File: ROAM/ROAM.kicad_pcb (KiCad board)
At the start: 4 copper layers, 90 x 56.8 mm, 11 parts, among them J1 CommanderX16Expansion Alt, U1 SST39SF040 (ROM), U2 74HCT00, U3 74HCT138, U4 AS6C4008 (RAM)

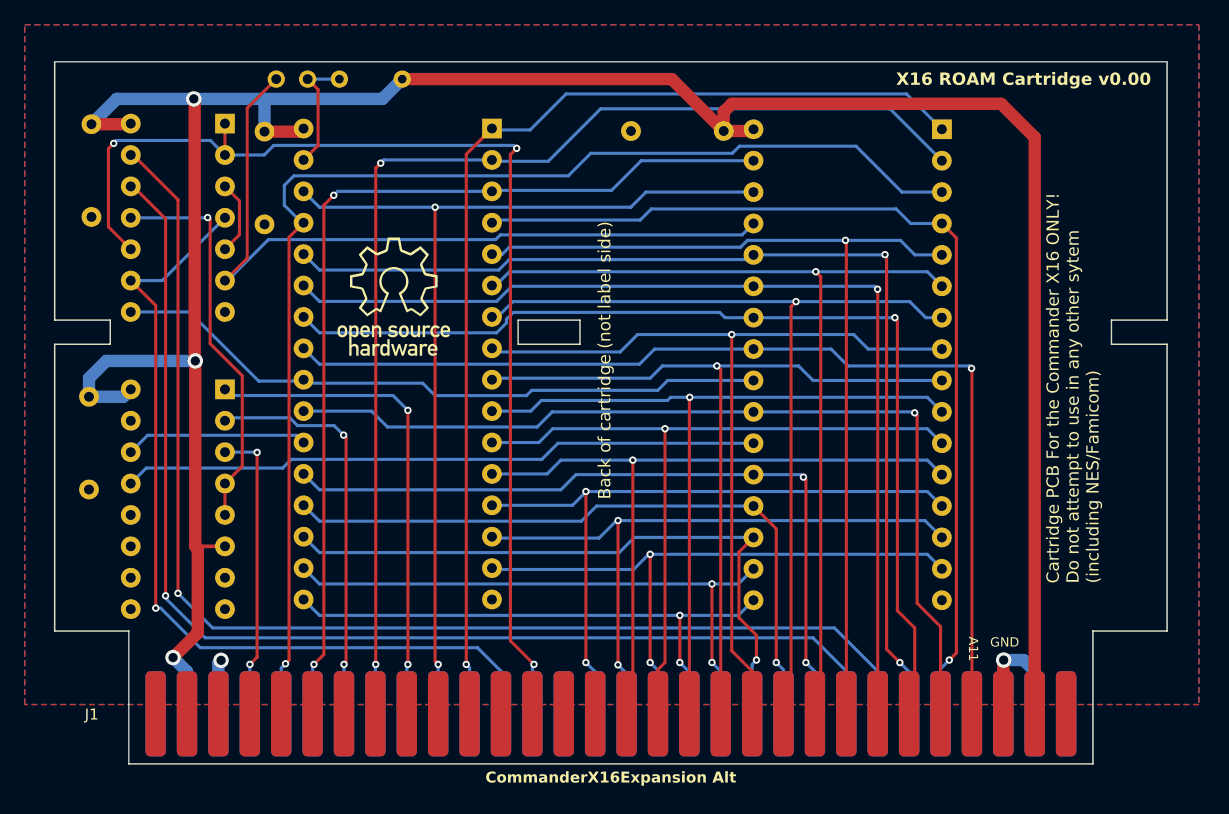
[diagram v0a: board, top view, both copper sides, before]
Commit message: Merged Wavicle's contributions to ROAM, added silk and some markup, updated readmed
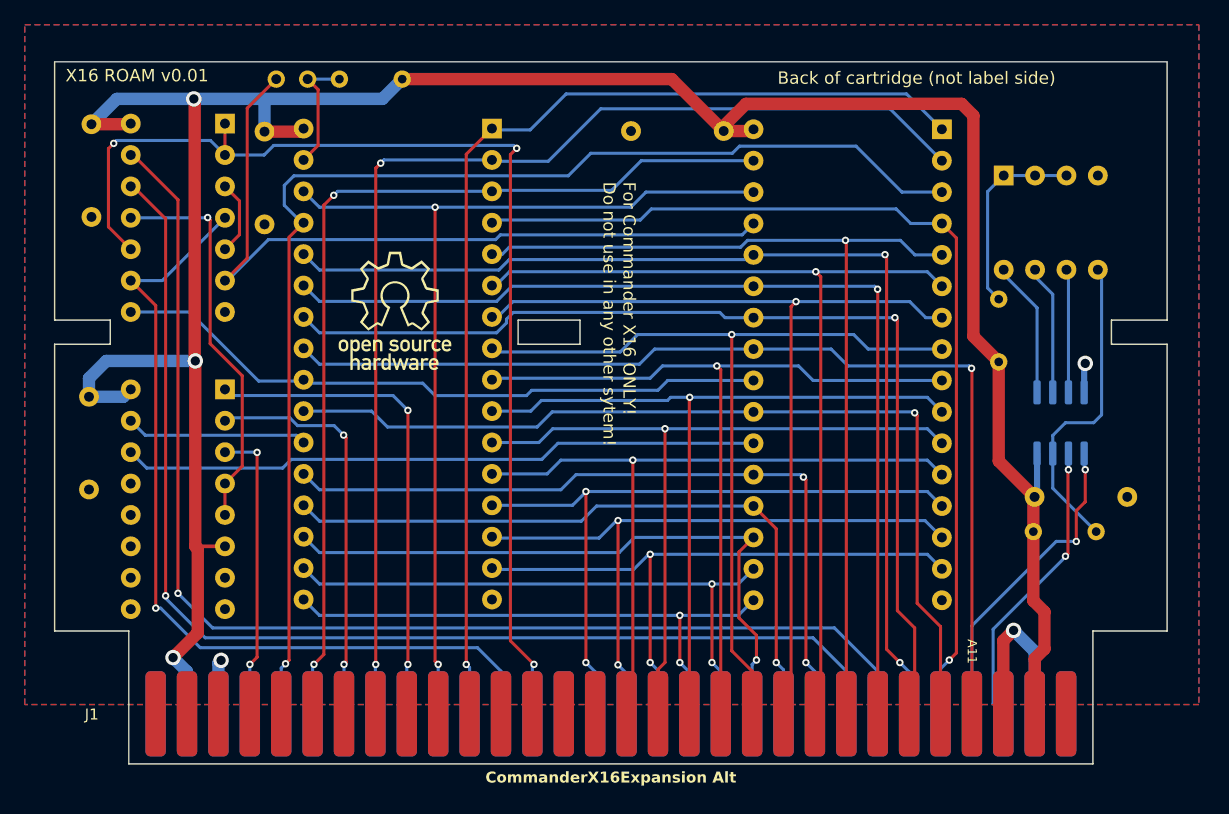
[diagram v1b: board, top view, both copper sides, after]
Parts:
- added C5: 100nF, Capacitor_THT:C_Axial_L3.8mm_D2.6mm_P7.50mm_Horizontal, B.Cu at (134.2, 113.2)
- added R2: 100K, Resistor_THT:R_Axial_DIN0204_L3.6mm_D1.6mm_P5.08mm_Horizontal, B.Cu at (131.7, 116.0)
- added R3: 100K, Resistor_THT:R_Axial_DIN0204_L3.6mm_D1.6mm_P5.08mm_Horizontal, B.Cu at (123.8, 102.3)
- added SW1: SW_DIP_x04, Button_Switch_THT:SW_DIP_SPSTx04_Slide_9.78x12.34mm_W7.62mm_P2.54mm, B.Cu at (124.2, 87.2)
- added U5: FM24C64B, Package_SO:SOIC-8_3.9x4.9mm_P1.27mm, B.Cu at (128.8, 107.2)
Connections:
- J1 pad 54: unconnected-(J1-SDA-Pad54) -> /SDA
- J1 pad 56: unconnected-(J1-SCL-Pad56) -> /SCL
- U3 pad 13: !RAMBEN -> unconnected-(U3-~{Y2}-Pad13)
- U3 pad 14: !ROMBEN -> !RAMBEN
- U3 pad 15: unconnected-(U3-~{Y0}-Pad15) -> !ROMBEN
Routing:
- net /SDA: track 0.00 -> 25.8 mm, vias 0 -> 2
- net /WP: track 0.00 -> 25.7 mm
- net /SCL: track 0.00 -> 23.6 mm, vias 0 -> 2
- net Net-(R3-Pad2): track 0.00 -> 16.0 mm
- net /FA0: track 0.00 -> 11.0 mm
- net /FA1: track 0.00 -> 10.5 mm
- net /FA2: track 0.00 -> 9.99 mm
- net GND: track 15.1 -> 21.3 mm, vias 2 -> 3
- net +5V: track 208.5 -> 210.3 mm
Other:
- board text added: "A0"
- board text added: "A1"
- board text added: "A2"
- board text added: "For Commander X16 ONLY! Do not use in any other sytem!"
- board text added: "NVRAM Addr"
- board text added: "NVRAM Wr. Prot."
- board text added: "X16 ROAM v0.01"
- board text removed: "Cartridge PCB For the Commander X16 ONLY! Do not attempt to use in any other sytem (including NES/Famicom)"
- board text removed: "GND"
- board text removed: "SCL"
- board text removed: "X16 ROAM Cartridge v0.00"

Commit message: Silk
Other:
- board text added: "5V"
- board text added: "A10"
- board text added: "A12"
- board text added: "A13"
- board text added: "A14"
- board text added: "A15"
- board text added: "A3"
- board text added: "A4"
- board text added: "A5"
- board text added: "A6"
- board text added: "A7"
- board text added: "A8"
- board text added: "A9"
- board text added: "D0"
- board text added: "D1"
- board text added: "D2"
- board text added: "D3"
- board text added: "D4"
- board text added: "D5"
- board text added: "D6"
- board text added: "D7"
- board text added: "Front of Cart Label side"
- board text added: "GND"
- board text added: "PHI2"
- board text added: "ROMB0"
- board text added: "ROMB1"
- board text added: "ROMB2"
- board text added: "ROMB3"
- board text added: "ROMB4"
- board text added: "ROMB5"
- board text added: "ROMB6"
- board text added: "ROMB7"
- board text added: "RWB"
- board text added: "SCL"
- board text added: "SDA"
- board text removed: "Front of cartridge, label side"

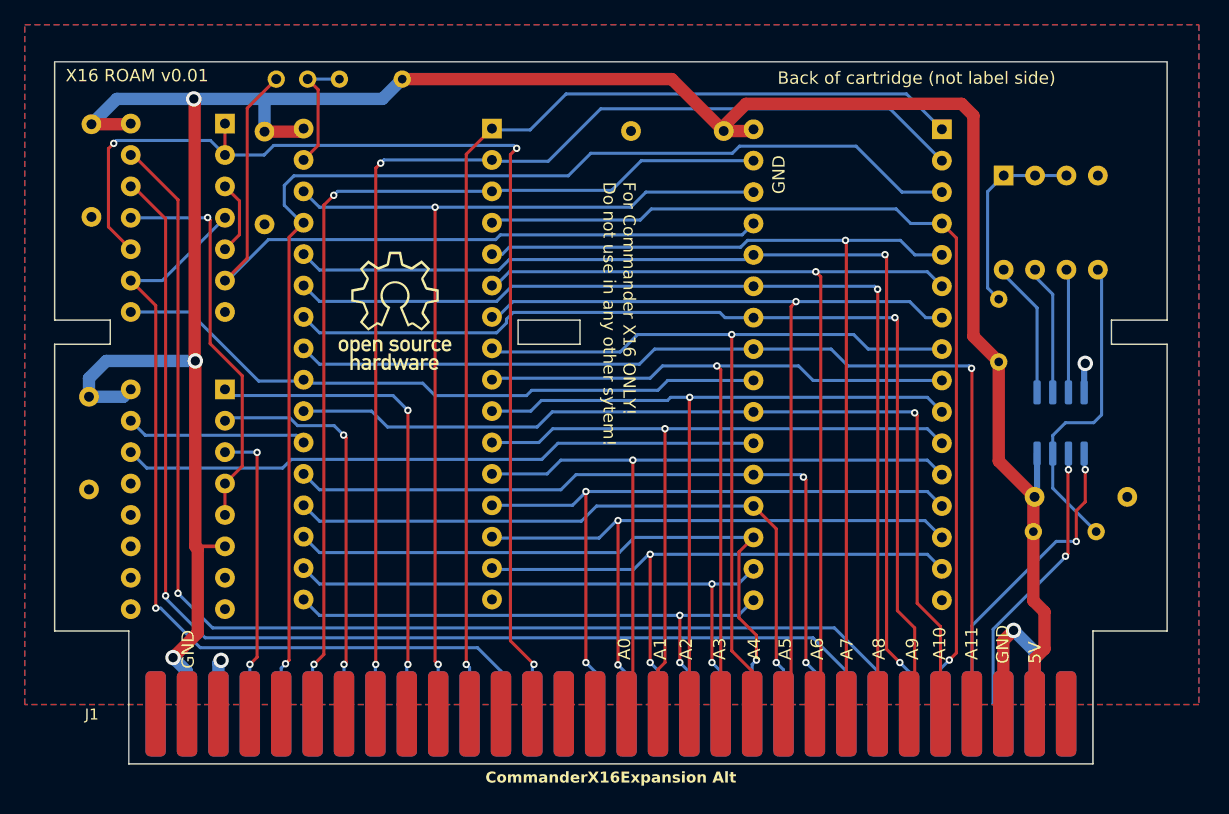
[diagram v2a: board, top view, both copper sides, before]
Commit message: Ported over Wavicle's latest changes
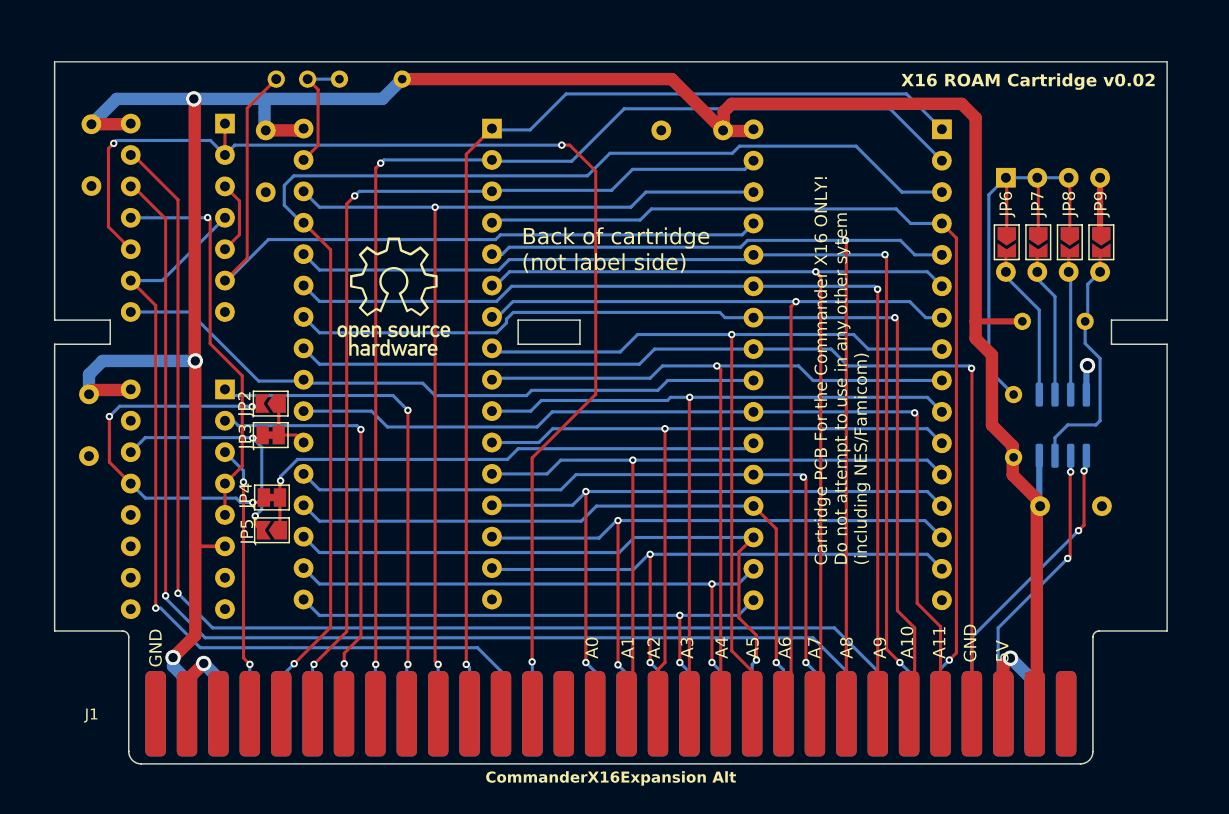
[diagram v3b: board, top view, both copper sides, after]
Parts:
- added JP2: BANK64_ROM, Jumper:SolderJumper-2_P1.3mm_Open_TrianglePad1.0x1.5mm, F.Cu at (64.9, 105.7)
- added JP3: BANK32_ROM, Jumper:SolderJumper-2_P1.3mm_Bridged_Pad1.0x1.5mm, F.Cu at (64.9, 108.2)
- added JP4: BANK64_RAM, Jumper:SolderJumper-2_P1.3mm_Bridged_Pad1.0x1.5mm, F.Cu at (65.0, 113.2)
- added JP5: BANK32_RAM, Jumper:SolderJumper-2_P1.3mm_Open_TrianglePad1.0x1.5mm, F.Cu at (65.0, 115.9)
- added JP6: JPFA0, Jumper:SolderJumper-2_P1.3mm_Open_TrianglePad1.0x1.5mm, F.Cu at (124.5, 92.6)
- added JP7: JPFA1, Jumper:SolderJumper-2_P1.3mm_Open_TrianglePad1.0x1.5mm, F.Cu at (127.0, 92.6)
- added JP8: JPFA2, Jumper:SolderJumper-2_P1.3mm_Open_TrianglePad1.0x1.5mm, F.Cu at (129.6, 92.6)
- added JP9: JPWP, Jumper:SolderJumper-2_P1.3mm_Open_TrianglePad1.0x1.5mm, F.Cu at (132.1, 92.6)
- C1, C2, C3, C4, C5: footprint Capacitor_THT:C_Axial_L3.8mm_D2.6mm_P7.50mm_Horizontal -> Capacitor_THT:C_Disc_D4.3mm_W1.9mm_P5.00mm
- J1: footprint CommanderX16Expansion:CommanderX16Cartridge -> X16Expansion:CommanderX16Cartridge
- moved R2 8.99 mm to (125.0, 110.0), turned to 90 degrees
- moved R3 7.72 mm to (130.8, 99.0), turned to 180 degrees
- moved C2 2.70 mm to (50.2, 109.9)
- moved C1 2.60 mm to (64.5, 88.5)
- moved C4 2.45 mm to (96.5, 83.5)
- moved C5 2.18 mm to (132.2, 114.0)
- moved U5 0.25 mm to (129.0, 107.4)
- moved SW1 0.25 mm to (124.4, 87.4)
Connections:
- R2 pad 1: /WP -> +5V
- R2 pad 2: +5V -> Net-(JP6-A)
- R3 pad 1: +5V -> /WP
- R3 pad 2: Net-(R3-Pad2) -> +5V
- SW1 pad 1: Net-(R3-Pad2) -> Net-(JP6-A)
- SW1 pad 2: Net-(R3-Pad2) -> Net-(JP6-A)
- SW1 pad 3: Net-(R3-Pad2) -> Net-(JP6-A)
- U3 pad 13: unconnected-(U3-~{Y2}-Pad13) -> Net-(JP2-B)
- U3 pad 14: !RAMBEN -> Net-(JP3-A)
- U3 pad 15: !ROMBEN -> unconnected-(U3-~{Y0}-Pad15)
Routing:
- net Net-(JP6-A): track 0.00 -> 37.3 mm
- net Net-(JP2-B): track 0.00 -> 30.0 mm, vias 0 -> 3
- net Net-(JP3-A): track 0.00 -> 19.3 mm, vias 0 -> 2
- net Net-(R3-Pad2): track 16.0 -> 0.00 mm
- net !ROMBEN: track 14.7 -> 4.73 mm
- net !RAMBEN: track 51.7 -> 43.1 mm, vias 0 -> 1
- net /RWB: track 92.4 -> 98.9 mm
- net /WP: track 25.7 -> 20.0 mm
- net GND: track 21.3 -> 17.9 mm
- net /ROMB6: track 32.4 -> 34.5 mm
- net /ROMB7: track 24.0 -> 22.0 mm
- net /FA2: track 9.99 -> 11.3 mm
- net /FA0: track 11.0 -> 12.3 mm
- net ROMB0: track 100.1 -> 99.0 mm
- net /SDA: track 25.8 -> 24.7 mm
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- removed copper zone on B.Cu, net GND
- removed copper zone on F.Cu, net GND
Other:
- outline, holes or cut-outs redrawn
- board text added: "1"
- board text added: "2"
- board text added: "4"
- board text added: "74HCT138"
- board text added: "AS6C4008 (RAM)"
- board text added: "Cartridge PCB For the Commander X16 ONLY! Do not attempt to use in any other sytem (including NES/Famicom)"
- board text added: "NVRAM Addr 0x50 +"
- board text added: "SST39SF040 (ROM)"
- board text added: "X16 ROAM Cartridge v0.02"
- board text removed: "For Commander X16 ONLY! Do not use in any other sytem!"
- board text removed: "NVRAM Addr"
- board text removed: "X16 ROAM v0.01"

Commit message: Tweaks to both Simplecart and ROAM
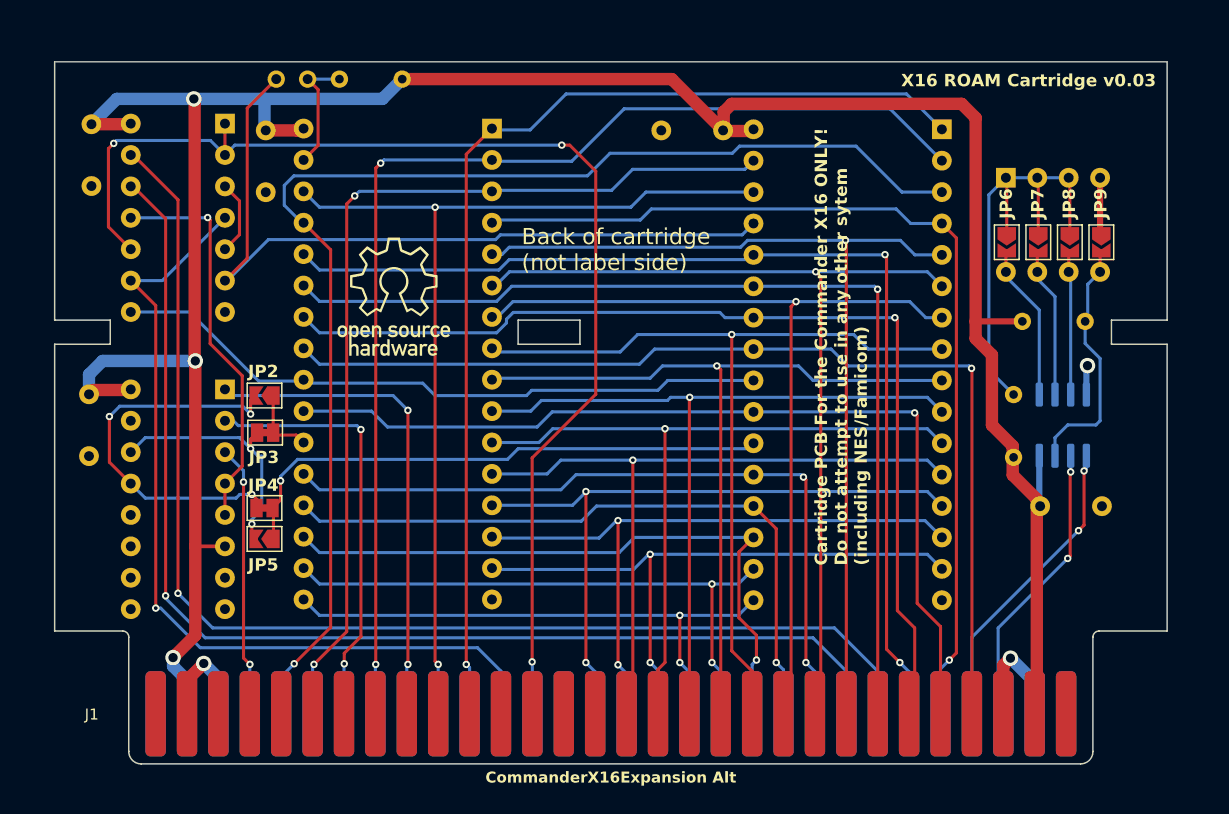
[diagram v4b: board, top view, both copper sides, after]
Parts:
- moved JP4 1.04 mm to (64.4, 114.1)
- moved JP5 0.92 mm to (64.4, 116.6)
- moved JP2 0.82 mm to (64.4, 105.0)
- moved JP3 0.49 mm to (64.5, 108.0)
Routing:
- net Net-(JP3-A): track 19.3 -> 20.5 mm
- net !RAMBEN: track 43.1 -> 44.2 mm
- net Net-(JP2-B): track 30.0 -> 31.1 mm
- net !ROMBEN: track 4.73 -> 5.27 mm
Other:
- board text added: "X16 ROAM Cartridge v0.03"
- board text removed: "5V"
- board text removed: "74HCT138"
- board text removed: "A0"
- board text removed: "A1"
- board text removed: "A10"
- board text removed: "A11"
- board text removed: "A12"
- board text removed: "A13"
- board text removed: "A14"
- board text removed: "A15"
- board text removed: "A2"
- board text removed: "A3"
- board text removed: "A4"
- board text removed: "A5"
- board text removed: "A6"
- board text removed: "A7"
- board text removed: "A8"
- board text removed: "A9"
- board text removed: "AS6C4008 (RAM)"
- board text removed: "D0"
- board text removed: "D1"
- board text removed: "D2"
- board text removed: "D3"
- board text removed: "D4"
- board text removed: "D5"
- board text removed: "D6"
- board text removed: "D7"
- board text removed: "GND"
- board text removed: "PHI2"
- board text removed: "ROMB0"
- board text removed: "ROMB1"
- board text removed: "ROMB2"
- board text removed: "ROMB3"
- board text removed: "ROMB4"
- board text removed: "ROMB5"
- board text removed: "ROMB6"
- board text removed: "ROMB7"
- board text removed: "RWB"
- board text removed: "SCL"
- board text removed: "SDA"
- board text removed: "SST39SF040 (ROM)"
- board text removed: "X16 ROAM Cartridge v0.02"

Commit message: 1uF Caps
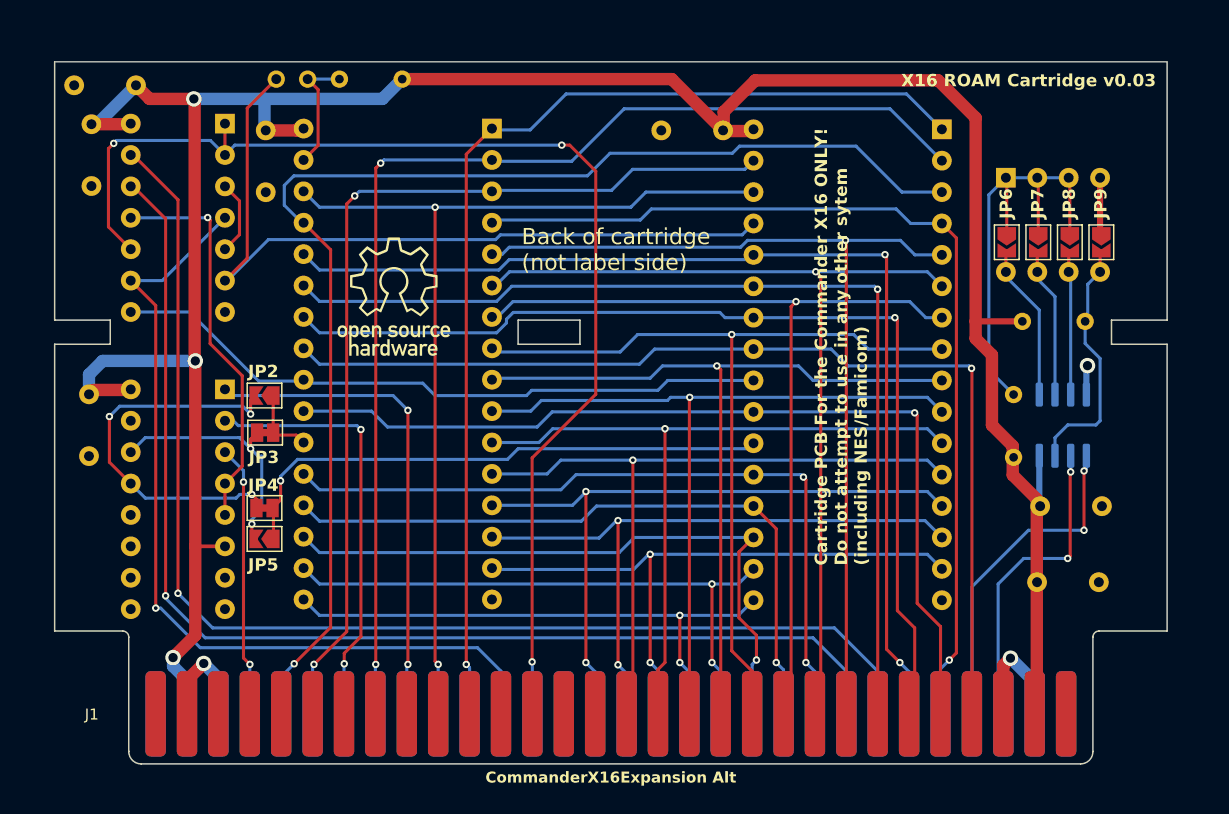
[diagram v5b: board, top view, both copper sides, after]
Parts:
- added C6: 1uF, Capacitor_THT:C_Disc_D4.3mm_W1.9mm_P5.00mm, B.Cu at (131.9, 120.1)
- added C7: 1uF, Capacitor_THT:C_Disc_D4.3mm_W1.9mm_P5.00mm, B.Cu at (49.0, 79.9)
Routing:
- net /SDA: track 24.7 -> 27.3 mm
- net +5V: track 210.5 -> 213.0 mm
- net /SCL: track 22.9 -> 25.0 mm

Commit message: Minor PCB updates, BOM
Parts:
- R1, R2, R3: footprint Resistor_THT:R_Axial_DIN0204_L3.6mm_D1.6mm_P5.08mm_Horizontal -> Resistor_THT:R_Axial_DIN0204_L3.6mm_D1.6mm_P7.62mm_Horizontal
- moved R1 1.03 mm to (71.5, 79.4)
- moved R3 0.82 mm to (131.6, 99.0)
- moved R2 0.58 mm to (124.5, 109.7)
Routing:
- net Net-(JP6-A): track 37.3 -> 35.6 mm
- net +5V: track 213.0 -> 211.3 mm

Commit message: Laying the ground work (har har)
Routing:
- net Net-(JP1-B): track 9.95 -> 11.0 mm
- net A5: track 69.9 -> 70.8 mm
- net Net-(JP6-A): track 35.6 -> 34.7 mm
- net GND: track 17.9 -> 17.0 mm, vias 3 -> 74
- net A2: track 63.0 -> 63.6 mm
- net /A15: track 95.4 -> 94.8 mm
- net A3: track 65.5 -> 66.0 mm
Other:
- board text added: "X16 ROAM Cartridge v0.04"
- board text removed: "X16 ROAM Cartridge v0.03"
